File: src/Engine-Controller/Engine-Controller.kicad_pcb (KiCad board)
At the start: 4 copper layers, 116.8 x 56.7 mm, 127 parts, among them J2 Jumper_NO, P1 EJ508A, P10 282837-2, P16 647676-2, P17 0530470410, P18 PPTC041LFBN-RC, P2 282837-6, P3 3220-20-0200-00, P4 Micro_SD_Card, P5 USB, P6 140-504-415-000, P7 647676-2, P8 20021511-00026T4LF, P9 5015680807, Q1 QS5U17TR, U1 STM32H750VBTx, U10 LMS8117AMP-3.3_NOPB, U11 TS391IYLT, U12 MAX4617EUE+T, U13 MAX4617EUE+T, U14 MCP96L01T-E_MX, U15 AD623ARZ-R7, U2 LM22672MRE-5.0_NOPB, U3 LMS8117AMP-3.3_NOPB, U4 SST25VF040B-50-4I-S2AE-T, U5 CP2102-GMR(QFN28), U6 TPS2115APWR, U7 MC74HC4066ADG, U8 AD623ARZ-R7, U9 MC74HC4066ADG, Y1 ECS-240-18-33-JGN-TR

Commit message: routed rev4
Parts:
- added R36: 10k, Engine-Controller:RES_0603, F.Cu at (138.3, 134.9)
- added R37: 10k, Engine-Controller:RES_0603, F.Cu at (113.0, 138.1)
- D8: value SP0504BAHTG -> SP0504BAHTG_LTF
- TP12, TP13, TP6, TP7, TP8, TP9: moved to B.Cu
- U11: value TS391IYLT -> SOT23-5_STM
- moved TP7 122.8 mm to (177.5, 136.0), turned to 180 degrees
- moved R18 121.9 mm to (169.7, 141.5), turned to 180 degrees
- moved R15 117.6 mm to (173.7, 141.5)
- moved TP6 117.4 mm to (176.7, 132.4), turned to 180 degrees
- moved TP12 117.0 mm to (180.7, 135.2), turned to 180 degrees
- moved TP9 112.5 mm to (183.1, 137.8), turned to 180 degrees
- moved C19 111.0 mm to (184.9, 129.6), turned to 90 degrees
- moved C20 110.8 mm to (183.1, 129.6), turned to 90 degrees
- moved TP13 94.9 mm to (177.1, 123.7), turned to 180 degrees
- moved R27 91.1 mm to (105.2, 129.7)
- moved TP8 88.0 mm to (118.4, 114.1), turned to 180 degrees
- moved C30 83.1 mm to (94.6, 139.3), turned to 90 degrees
- moved C28 82.1 mm to (124.0, 123.1), turned to -90 degrees
- moved R28 79.2 mm to (130.8, 127.5), turned to 180 degrees
- moved C27 76.3 mm to (137.2, 120.2), turned to -90 degrees
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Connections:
- R18 pad 1: SWDIO -> SWCLK
- U1 pad 38: SP_CONT -> NOZ_CONT
- U1 pad 39: NOZ_CONT -> SP_CONT
- U12 pad 6: (no net) -> Earth
- U13 pad 6: (no net) -> Earth
- U7 pad 14: 3.3V -> A3.3V
- U9 pad 14: 3.3V -> A3.3V
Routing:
- net 5V: track 160.2 -> 342.8 mm, vias 1 -> 7
- net VIN: track 104.7 -> 209.9 mm, vias 2 -> 3
- net Earth: track 150.8 -> 245.0 mm, vias 29 -> 40
- net SP_CONT: track 0.00 -> 93.0 mm, vias 0 -> 6
- net E_CONT: track 0.00 -> 88.2 mm, vias 0 -> 8
- net PT_MUX_A: track 0.00 -> 85.3 mm, vias 0 -> 3
- net NOZ_CONT: track 0.00 -> 84.7 mm, vias 0 -> 6
- net PT_MUX_C: track 0.00 -> 83.4 mm, vias 0 -> 5
- net PT_MUX_B: track 0.00 -> 82.0 mm, vias 0 -> 4
- net FIRE: track 0.00 -> 79.7 mm, vias 0 -> 4
- net PT_GAIN1: track 0.00 -> 64.8 mm, vias 0 -> 4
- net PT_GAIN7: track 0.00 -> 64.6 mm, vias 0 -> 4
- net PT_GAIN2: track 0.00 -> 63.8 mm, vias 0 -> 4
- net PT_GAIN4: track 0.00 -> 63.7 mm, vias 0 -> 2
- net PT_GAIN5: track 0.00 -> 63.1 mm, vias 0 -> 2
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- added copper zone on In2.Cu, net A3.3V
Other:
- board text added: "APOWER"
- board text added: "SWITCH"

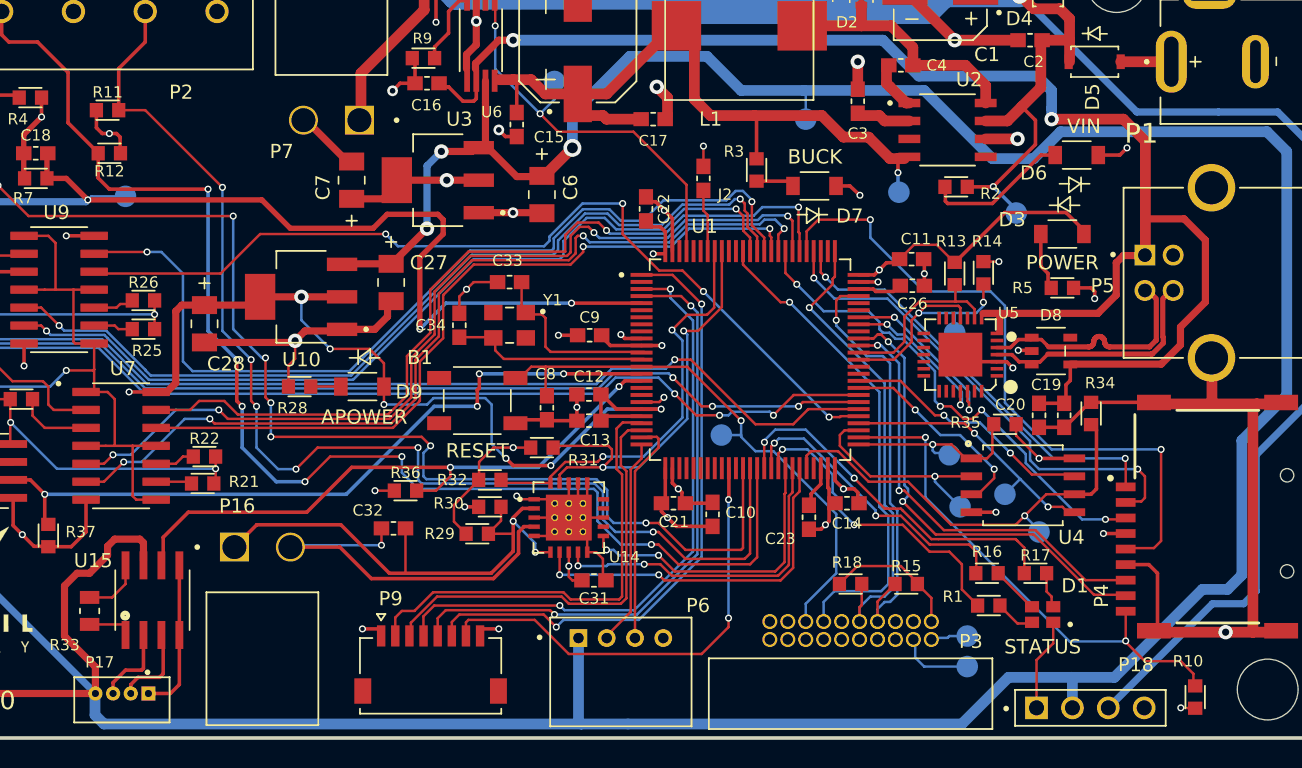
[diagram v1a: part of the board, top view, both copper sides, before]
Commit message: resolved minor DRC errors
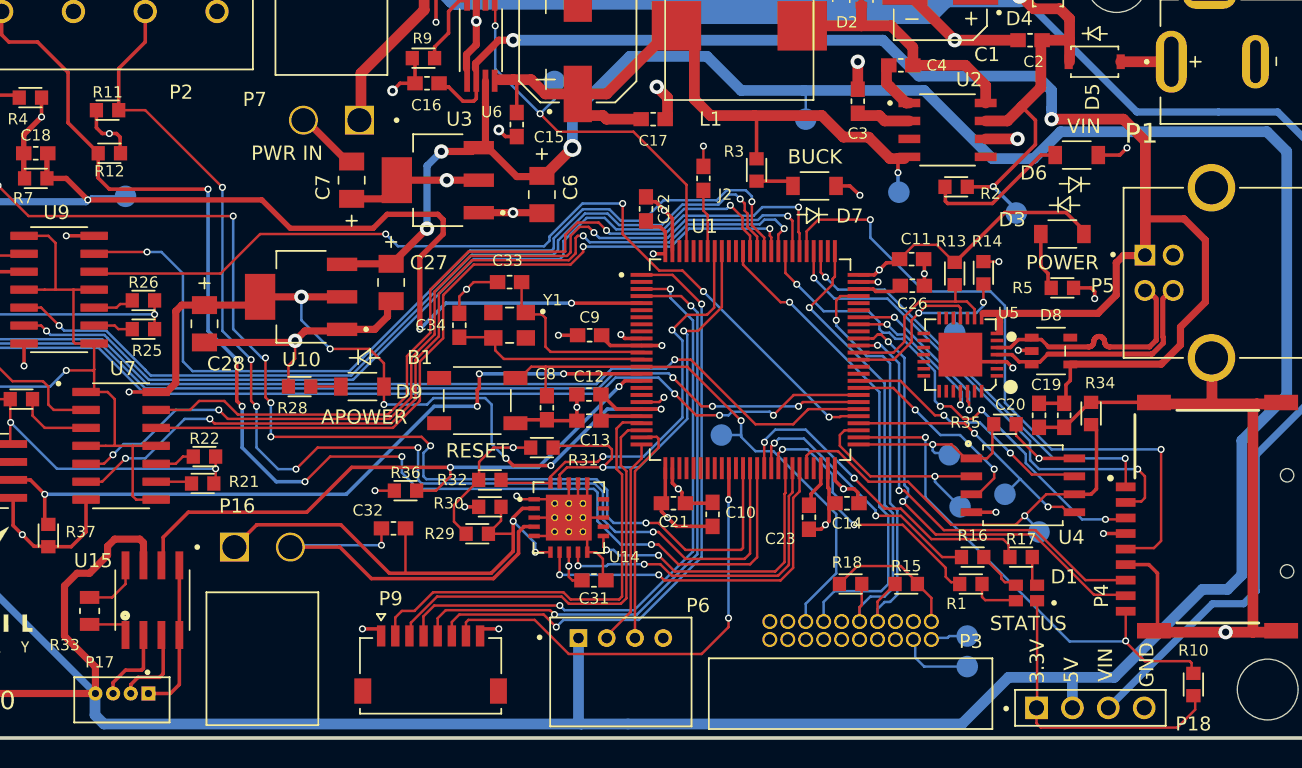
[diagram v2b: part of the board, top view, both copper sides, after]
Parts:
- moved R1 1.98 mm to (178.3, 141.5)
- moved D1 1.91 mm to (182.2, 142.1)
- moved R16 1.53 mm to (178.4, 139.6)
- moved R17 1.53 mm to (181.8, 139.6)
- moved R10 0.90 mm to (194.0, 148.6)
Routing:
- net 3.3V: track 94.8 -> 108.2 mm, vias 16 -> 15
- net STATUS_G: track 21.6 -> 18.8 mm
- net STATUS_B: track 22.1 -> 19.3 mm
- net STATUS_R: track 25.9 -> 23.5 mm
- net SD_DETECT: track 36.0 -> 35.3 mm
- net PT_GAIN2: track 63.8 -> 63.2 mm
- net Net-(D1-Pad2): track 2.80 -> 3.40 mm
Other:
- board text added: "3.3V"
- board text added: "5V"
- board text added: "E-MATCH"
- board text added: "GND"
- board text added: "NOZZLE"
- board text added: "PWR IN"
- board text added: "SOLID PROP"
- board text removed: "E-match"
- board text removed: "Nozzle"
- board text removed: "Solid Prop."

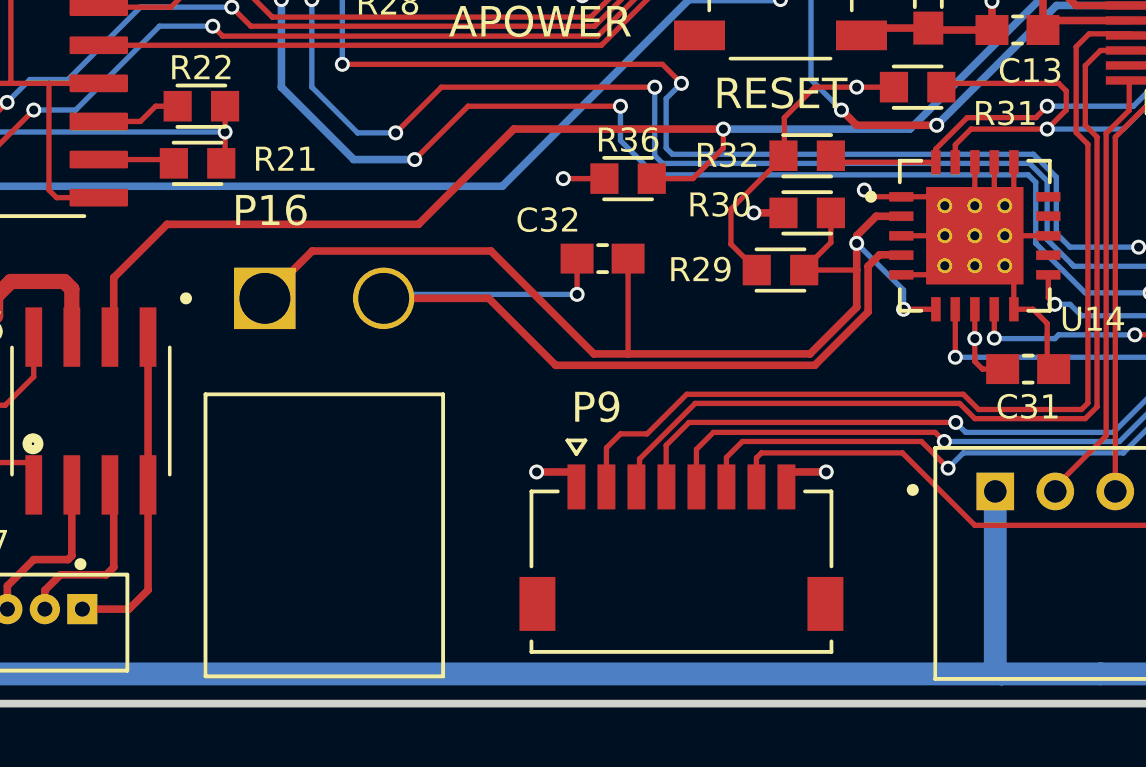
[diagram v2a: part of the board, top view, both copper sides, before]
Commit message: changed TC connector to be different from power connector
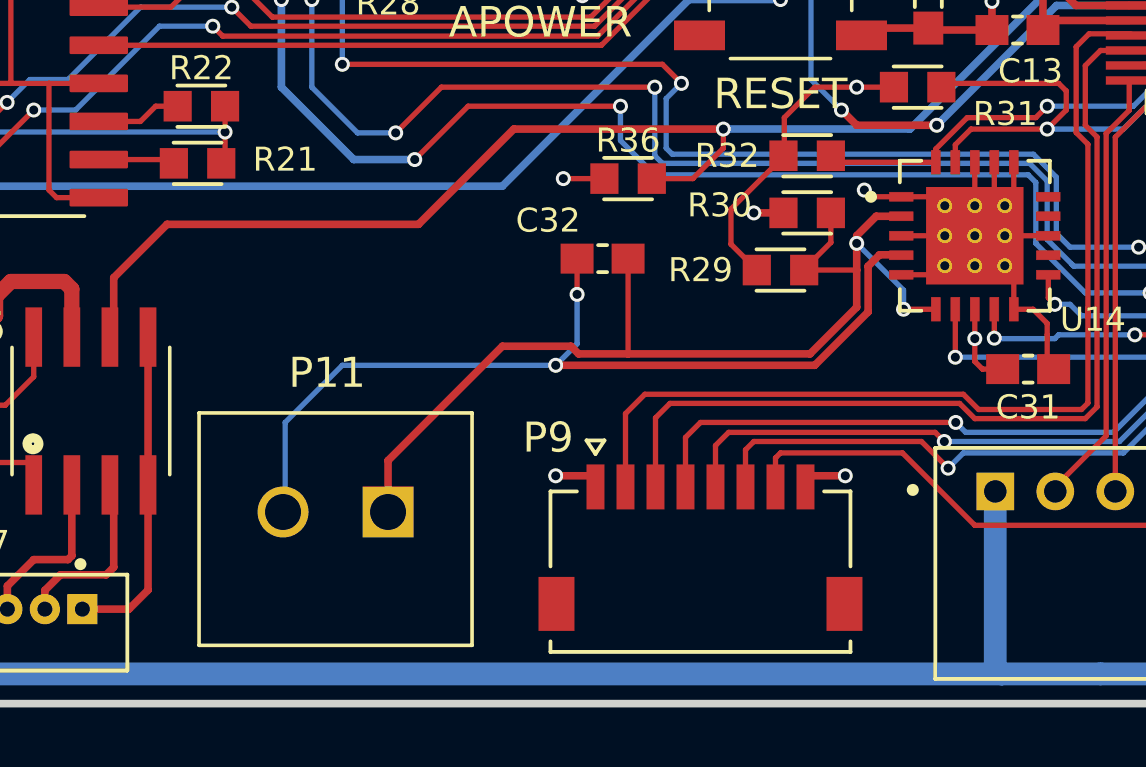
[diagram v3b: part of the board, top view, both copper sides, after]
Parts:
- removed P16: 647676-2, Engine-Controller:647676-2
- added P11: CON_532580229_MOL, Engine-Controller:532580229, F.Cu at (130.3, 146.0)
- D8: value SP0504BAHTG_LTF -> SP0504BAHTG
- U11: value SOT23-5_STM -> TS391IYLT
- moved P9 0.63 mm to (140.7, 147.7)
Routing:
- net /Sensors/TC+: track 37.2 -> 34.6 mm
- net /Sensors/TC-: track 27.9 -> 30.2 mm, vias 1 -> 2
- net W_RX: track 30.0 -> 30.8 mm
- net W_SS: track 32.7 -> 32.0 mm
- net W_MOSI: track 43.3 -> 42.7 mm
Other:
- board text added: "LOAD CELL"
- board text added: "LOX TANK TC"
- board text added: "PROGRAMMER"
- board text added: "VALVE CNTRL"

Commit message: updated README description
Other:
- board text added: "PRESSURE TRANSDUCERS"
- board text added: "TELEMETRY"
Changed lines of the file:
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@@
+    (effects (font (size 1.016 1.016) (thickness 0.2032)) (justify mirror))
+  )
+  (gr_text "PRESSURE TRANSDUCERS" (at 94.1832 129.9464 270) (layer "B.SilkS")
     (effects (font (size 1.016 1.016) (thickness 0.2032)) (justify mirror))
   )
@@
     (effects (font (size 1.016 1.016) (thickness 0.2032)))
   )
+  (gr_text "TELEMETRY" (at 140.9192 142.5194) (layer "F.SilkS")
+    (effects (font (size 1.016 1.016) (thickness 0.2032)))
+  )

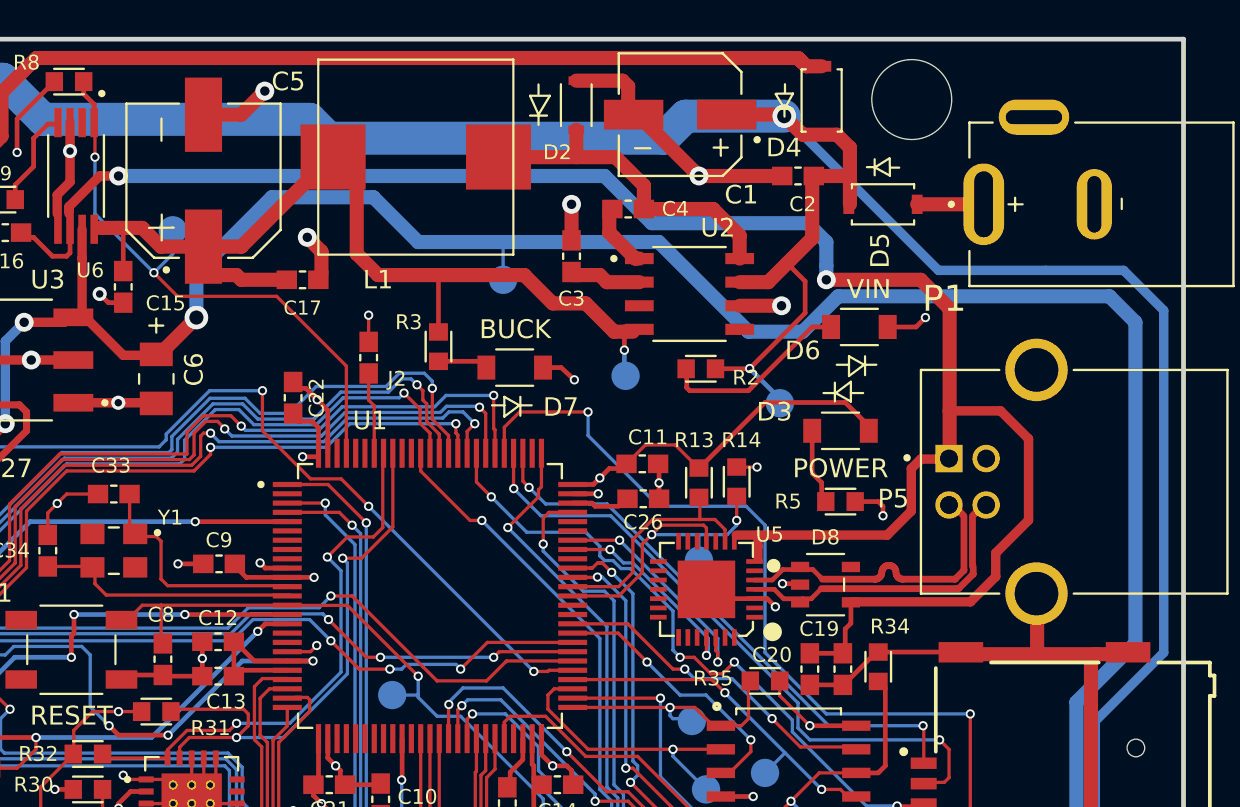
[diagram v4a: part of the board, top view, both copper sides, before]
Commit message: moved uart chip decoupling capacitors closer to IC pins
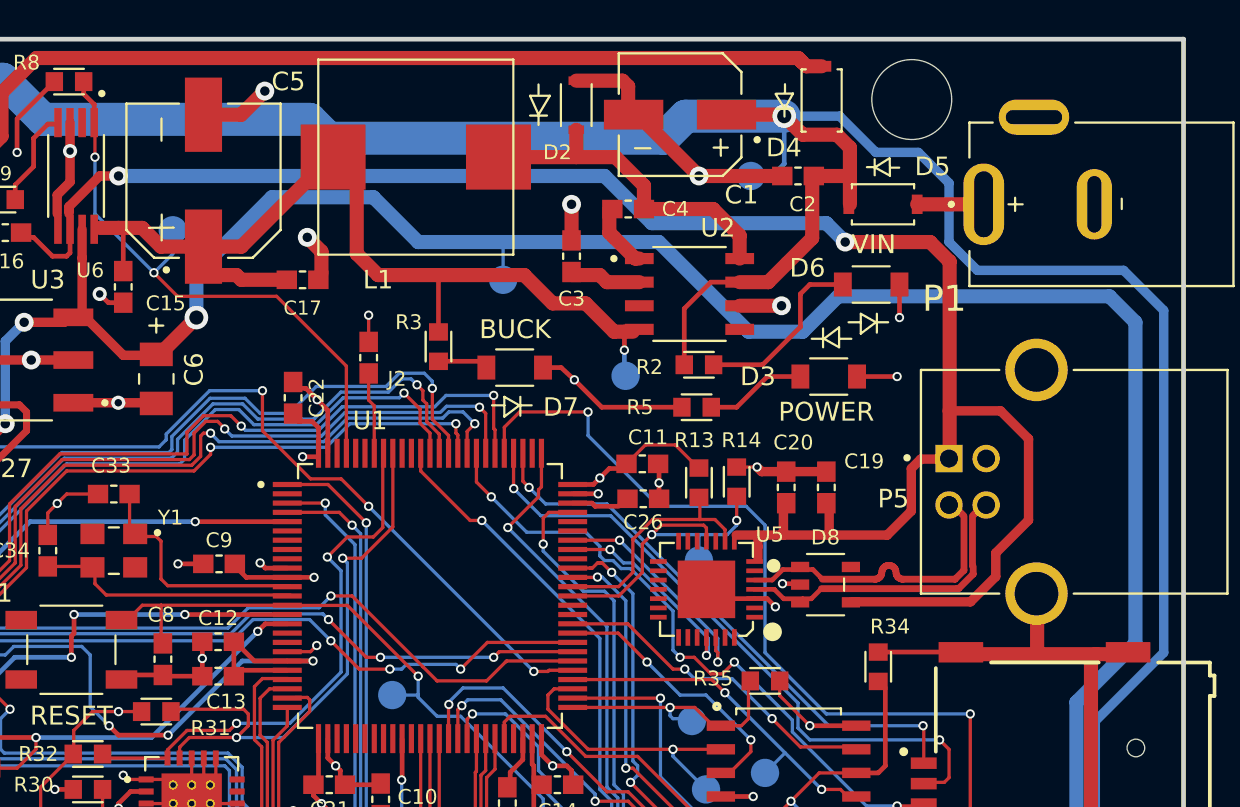
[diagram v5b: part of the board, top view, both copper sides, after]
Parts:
- D4, D5: value SM5819PL-TP -> SOD-123FL_MCC
- D8: value SP0504BAHTG -> SP0504BAHTG_LTF
- Q1: value QS5U17TR -> TRANS_QS5K_ROM
- moved TP2 12.3 mm to (179.9, 103.0)
- moved C20 9.86 mm to (181.8, 119.8), turned to -90 degrees
- moved C19 9.82 mm to (184.0, 119.8), turned to -90 degrees
- moved R5 9.26 mm to (177.0, 115.5), turned to 180 degrees
- moved D3 2.99 mm to (184.1, 113.8)
- moved D6 2.37 mm to (186.4, 108.9)
- moved R2 0.24 mm to (177.1, 113.2), turned to 0 degrees
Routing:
- net 3.3V: track 107.7 -> 99.1 mm, vias 15 -> 16
- net Earth: track 244.6 -> 248.4 mm, vias 40 -> 39
- net VIN: track 209.9 -> 211.5 mm, vias 3 -> 2
- net Net-(D3-Pad1): track 4.02 -> 5.48 mm
- net 5V_USB: track 106.3 -> 105.3 mm
- net Net-(D6-Pad2): track 10.2 -> 9.66 mm

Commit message: completed rev 5.0 layout
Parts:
- removed R22, R23, R24, R25, R26, R27: 1k, Engine-Controller:RES_0603
- removed U7, U9: MC74HC4066ADG, Engine-Controller:MC74HC4066ADG
- added J1: Jumper_NO, Engine-Controller:Jumper-NO, F.Cu at (132.2, 138.3)
- added R38: 2M, Engine-Controller:RES_0603, F.Cu at (125.9, 138.1)
- C11, C13, C14, C21, C22, C8, C9: value 0.1u -> 0.1uF
- D4, D5: value SOD-123FL_MCC -> SM5819PL-TP
- D8: value SP0504BAHTG_LTF -> SP0504BAHTG
- P11: value CON_532580229_MOL -> 282837-2; footprint Engine-Controller:532580229 -> Engine-Controller:282837-2
- Q1: value TRANS_QS5K_ROM -> QS5U17TR
- R19: value 1k -> 3.3k; footprint Engine-Controller:RES_0603 -> Engine-Controller:RES_0805
- R20, R6: value 1k -> 10k
- R21: value 1k -> 20k
- moved R21 15.8 mm to (118.8, 119.4)
- moved R20 9.78 mm to (118.8, 122.5), turned to 0 degrees
- moved P11 1.91 mm to (128.3, 145.8)
- moved R19 1.73 mm to (108.3, 127.5), turned to 0 degrees
- moved U15 0.38 mm to (120.0, 142.6)
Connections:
- B1 pad 1: Earth -> Net-(J1-B)
- P8 pad 14: PT5- -> Earth
- P8 pad 16: PT6- -> Earth
- P8 pad 18: PT7- -> Earth
- P8 pad 20: PT8- -> Earth
- P8 pad 3: 5V -> VIN
- P8 pad 4: 5V -> VIN
- R19 pad 1: Net-(R19-Pad1) -> Net-(U8--RG)
- R19 pad 2: Net-(R19-Pad2) -> Net-(U8-+RG)
- R20 pad 1: Net-(R20-Pad1) -> 5V_USB
- R20 pad 2: Net-(R19-Pad2) -> USB_DETECT
- R21 pad 1: Net-(R21-Pad1) -> Earth
- R21 pad 2: Net-(R19-Pad2) -> USB_DETECT
- U1 pad 17: unconnected-(U1-Pad17) -> PT5+
- U1 pad 18: unconnected-(U1-Pad18) -> PT6+
- U1 pad 3: W_MISO -> FIRE
- U1 pad 32: unconnected-(U1-Pad32) -> PT7+
- U1 pad 33: unconnected-(U1-Pad33) -> PT8+
- U1 pad 4: W_MOSI -> W_MISO
- U1 pad 5: FIRE -> W_MOSI
- U1 pad 55: PT_GAIN7 -> unconnected-(U1-PD8-Pad55)
- U1 pad 81: PT_GAIN0 -> USB_DETECT
- U1 pad 82: PT_GAIN1 -> unconnected-(U1-PD1-Pad82)
- U1 pad 84: PT_GAIN2 -> unconnected-(U1-PD3-Pad84)
- U1 pad 85: PT_GAIN3 -> unconnected-(U1-PD4-Pad85)
- U1 pad 86: PT_GAIN4 -> unconnected-(U1-PD5-Pad86)
- U1 pad 87: PT_GAIN5 -> unconnected-(U1-PD6-Pad87)
- U1 pad 88: PT_GAIN6 -> unconnected-(U1-PD7-Pad88)
- U12 pad 1: PT5+ -> unconnected-(U12-X4-Pad1)
- U12 pad 2: PT7+ -> unconnected-(U12-X6-Pad2)
- U12 pad 4: PT8+ -> unconnected-(U12-X7-Pad4)
- U12 pad 5: PT6+ -> unconnected-(U12-X5-Pad5)
- U13 pad 1: PT5- -> unconnected-(U13-X4-Pad1)
- U13 pad 2: PT7- -> unconnected-(U13-X6-Pad2)
- U13 pad 4: PT8- -> unconnected-(U13-X7-Pad4)
- U13 pad 5: PT6- -> unconnected-(U13-X5-Pad5)
- U8 pad 1: Net-(R27-Pad1) -> Net-(U8--RG)
- U8 pad 8: Net-(R19-Pad2) -> Net-(U8-+RG)
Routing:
- net PT8+: track 4.10 -> 78.0 mm, vias 0 -> 1
- net PT7+: track 5.97 -> 77.7 mm
- net PT6+: track 4.84 -> 70.0 mm, vias 0 -> 1
- net PT_GAIN1: track 64.8 -> 0.00 mm, vias 4 -> 0
- net PT_GAIN7: track 64.6 -> 0.00 mm, vias 4 -> 0
- net PT_GAIN4: track 63.9 -> 0.00 mm, vias 2 -> 0
- net PT_GAIN5: track 63.4 -> 0.00 mm, vias 2 -> 0
- net PT_GAIN2: track 63.2 -> 0.00 mm, vias 4 -> 0
- net PT_GAIN6: track 61.2 -> 0.00 mm, vias 2 -> 0
- net PT_GAIN0: track 60.1 -> 0.00 mm, vias 2 -> 0
- net Net-(R19-Pad2): track 57.5 -> 0.00 mm, vias 4 -> 0
- net PT_GAIN3: track 54.5 -> 0.00 mm, vias 2 -> 0
- net USB_DETECT: track 0.00 -> 53.5 mm, vias 0 -> 2
- net PT5+: track 13.0 -> 66.4 mm, vias 0 -> 1
- net Net-(R27-Pad1): track 50.2 -> 0.00 mm, vias 2 -> 0
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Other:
- board text added: "+"
- board text added: "-"

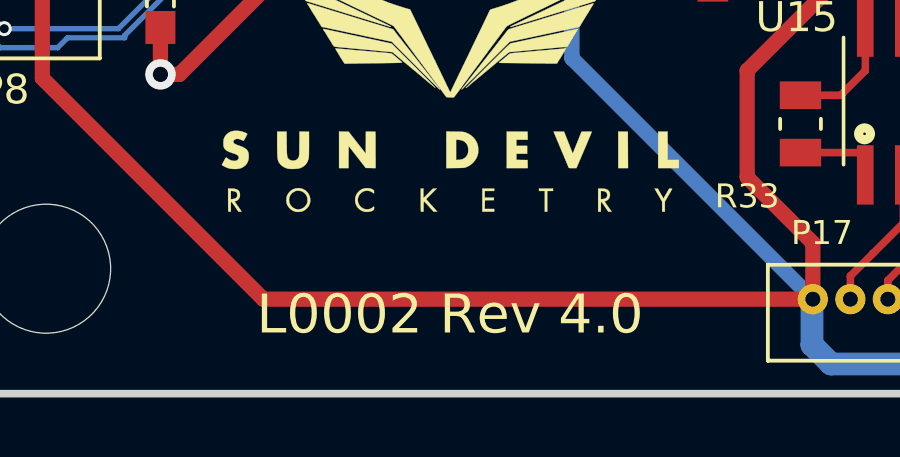
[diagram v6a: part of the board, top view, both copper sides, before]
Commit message: removed wireless interface connector
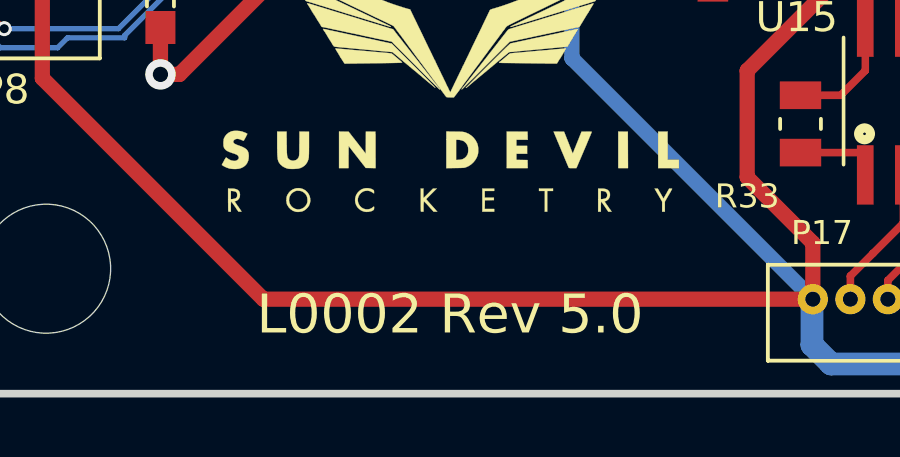
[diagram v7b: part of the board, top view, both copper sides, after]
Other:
- board text added: "L0002 Rev 5.0"
- board text removed: "L0002 Rev 4.0"
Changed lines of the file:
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@@
     (effects (font (size 1.016 1.016) (thickness 0.15)))
   )
-  (gr_text "L0002 Rev 4.0" (at 104.2162 149.7584) (layer "F.SilkS")
+  (gr_text "L0002 Rev 5.0" (at 104.2162 149.7584) (layer "F.SilkS")
     (effects (font (size 1.3 1.3) (thickness 0.2)))
   )
